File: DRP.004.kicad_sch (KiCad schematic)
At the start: 0 parts

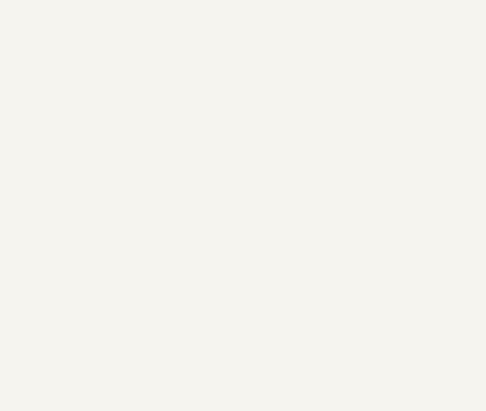
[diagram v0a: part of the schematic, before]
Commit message: Adjusted stencil for custom jig
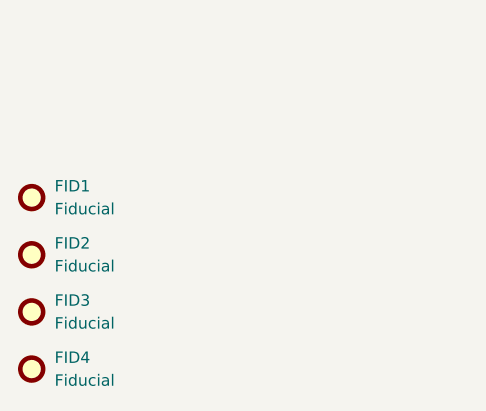
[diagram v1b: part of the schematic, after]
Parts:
- added FID1, FID2, FID3, FID4: Fiducial, Fiducial:Fiducial_0.5mm_Mask1.5mm, symbol Mechanical:Fiducial

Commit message: Finished v3
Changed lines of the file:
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@@
+		)
+	)
+	(symbol
+		(lib_id "Graphic:SYM_Flash_Large")
+		(at 254 156.21 0)
+		(unit 1)
+		(exclude_from_sim no)
+		(in_bom no)
+		(on_board yes)
+		(dnp no)
+		(property "Reference" "#SYM1"
+			(at 250.19 156.21 90)
+			(effects
+				(font
+					(size 1.27 1.27)
+				)
+				(hide yes)
+			)
+		)
+		(property "Value" "SYM_Flash_Large"
+			(at 257.302 156.21 90)
+			(effects
+				(font
+					(size 1.27 1.27)
+				)
+				(hide yes)
+			)
+		)
+		(property "Footprint" "Symbol:Symbol_HighVoltage_NoTriangle_2x5mm_Copper"
+			(at 253.238 163.576 0)
+			(effects
+				(font
+					(size 1.27 1.27)
+				)
+				(hide yes)
+			)
+		)
+		(property "Datasheet" "~"
+			(at 264.16 158.75 0)
+			(effects
+				(font
+					(size 1.27 1.27)
+				)
+				(hide yes)
+			)
+		)
+		(property "Description" "Flash symbol, large"
+			(at 254 156.21 0)
+			(effects
+				(font
+					(size 1.27 1.27)
+				)
+				(hide yes)
+			)
+		)
+		(property "Sim.Enable" "0"
+			(at 254 156.21 0)
+			(effects
+				(font
+					(size 1.27 1.27)
+				)
+				(hide yes)
+			)
+		)
+		(instances
+			(project ""
+				(path "/990f0ec4-1b5b-4db8-8f39-ecd88fffeea0"
+					(reference "#SYM1")
+					(unit 1)
+				)
+			)
 		)
 	)

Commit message: Expanded documentation
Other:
- note added: "${/990f0ec4-1b5b-4db8-8f39-ecd88fffeea0/6cce2e90-e51c-4942-a042-f4f9f078d271/66d2800e-8fce-4636-a04a-70d2094956bb:VALUE} Output: 3.0v - 4.4v Input USB: 5v Input BATT: 3.0v - 4.2v"
- note added: "${/990f0ec4-1b5b-4db8-8f39-ecd88fffeea0/9a8ba87a-c59f-4592-a0ef-e35d3bfde58d/a8d7b234-8ac0-468a-a976-6151f63ea50d:VALUE} FLASH: 32k RAM: 8k"
- note added: "1S Li-ion"
- note added: "BOOST ${/990f0ec4-1b5b-4db8-8f39-ecd88fffeea0/6cce2e90-e51c-4942-a042-f4f9f078d271/1bd17bee-2f02-427f-b24e-c0fc4b2c4825:VALUE} 5.5v"
- note added: "BUTTON"
- note added: "LDO ${/990f0ec4-1b5b-4db8-8f39-ecd88fffeea0/6cce2e90-e51c-4942-a042-f4f9f078d271/c47a5d3b-33a9-403c-a3ad-31fcb81bff44:VALUE} 1.8v 600mA"
- note added: "LEDs"
- note added: "SERVO"
- note added: "Slider switch + Power latch"
- note added: "USB"

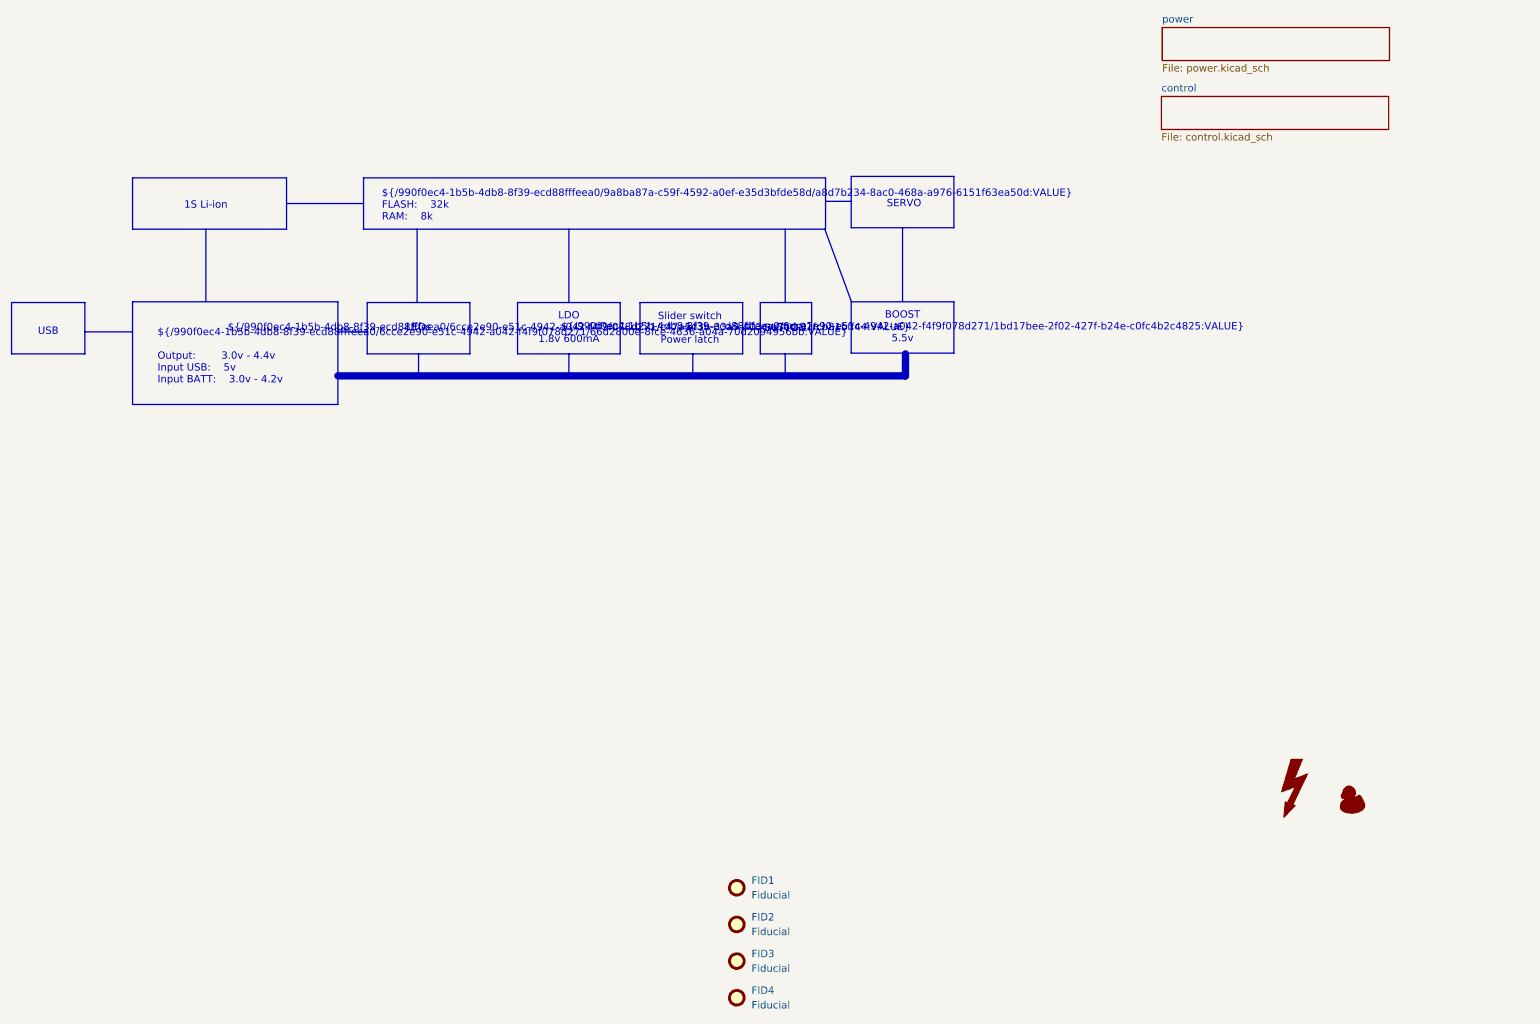
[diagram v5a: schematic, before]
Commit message: Updated schematics. Calculated inductor values
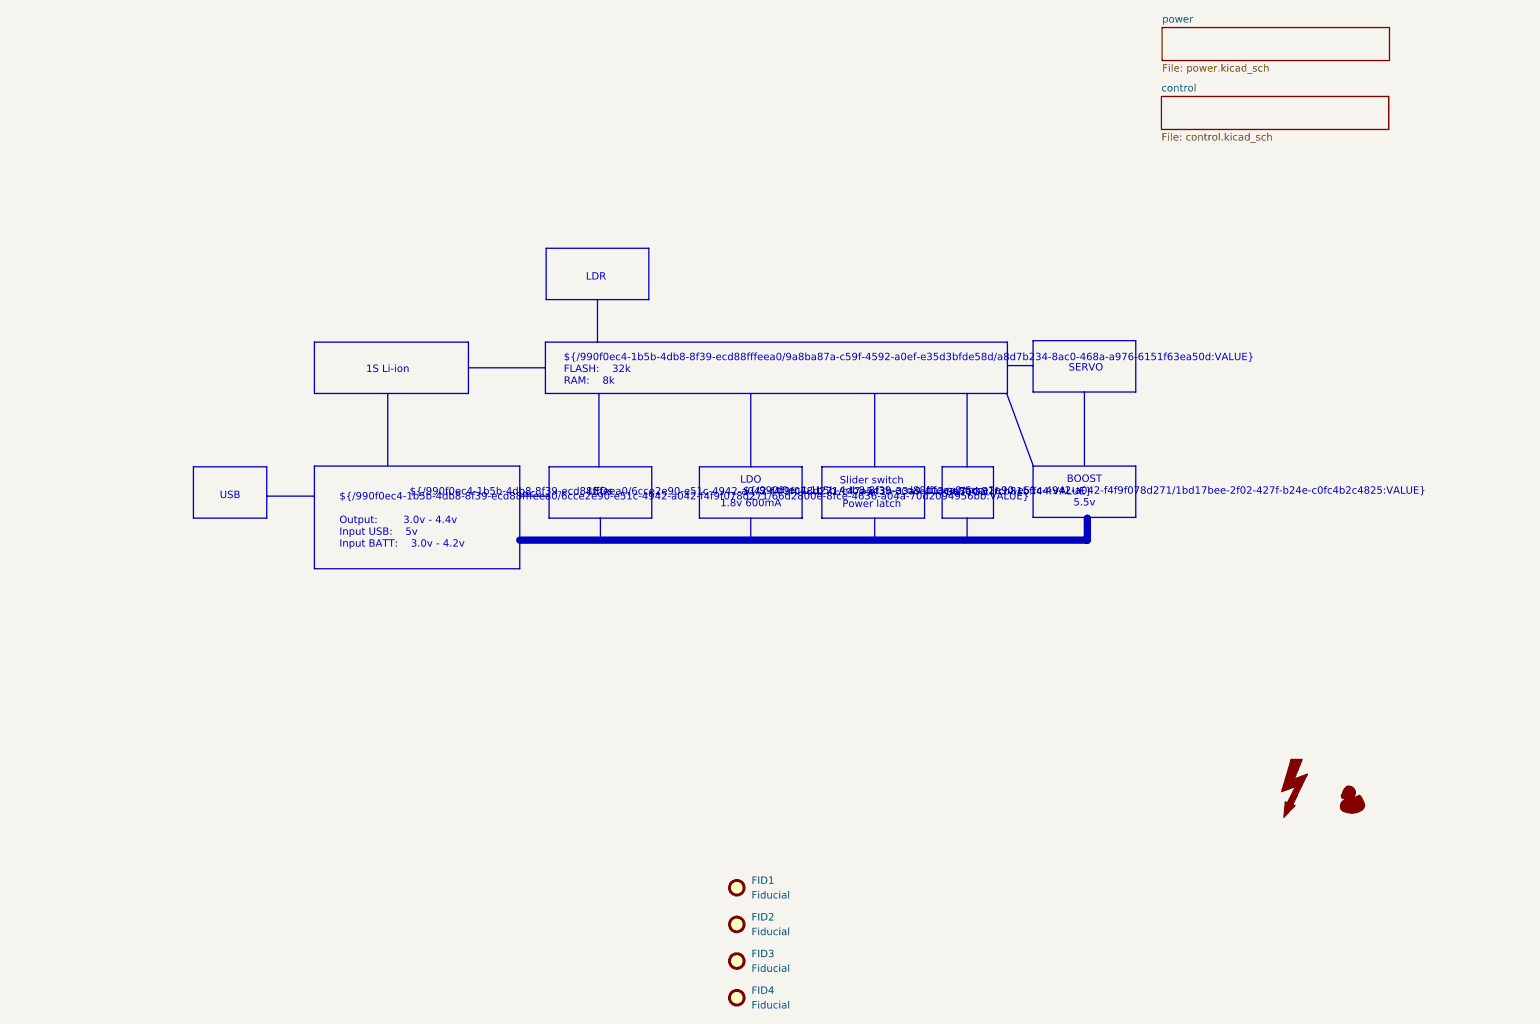
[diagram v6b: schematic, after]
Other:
- note added: "LDR"
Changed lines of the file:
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@@
 	)
 	(rectangle
-		(start 52.832 51.054)
-		(end 79.502 59.944)
+		(start 84.328 79.502)
+		(end 110.998 88.392)
 		(stroke
 			(width 0)
@@
 	)
 	(rectangle
-		(start 177.292 72.517)
-		(end 195.072 81.407)
+		(start 208.788 100.965)
+		(end 226.568 109.855)
 		(stroke
 			(width 0)
@@
 	)
 	(rectangle
-		(start 52.832 72.517)
-		(end 88.392 90.297)
+		(start 84.328 100.965)
+		(end 119.888 118.745)
 		(stroke
 			(width 0)
@@
 	)
 	(rectangle
-		(start 177.292 50.8)
-		(end 195.072 59.69)
+		(start 208.788 79.248)
+		(end 226.568 88.138)
 		(stroke
 			(width 0)
@@
 	)
 	(rectangle
-		(start 31.877 72.644)
-		(end 44.577 81.534)
+		(start 63.373 101.092)
+		(end 76.073 109.982)
 		(stroke
 			(width 0)
@@
 	)
 	(rectangle
-		(start 119.507 72.644)
-		(end 137.287 81.534)
+		(start 151.003 101.092)
+		(end 168.783 109.982)
 		(stroke
 			(width 0)
@@
 	)
 	(rectangle
-		(start 93.472 72.644)
-		(end 111.252 81.534)
+		(start 124.968 101.092)
+		(end 142.748 109.982)
 		(stroke
 			(width 0)
@@
 	)
 	(rectangle
-		(start 161.544 72.644)
-		(end 170.434 81.534)
+		(start 193.04 101.092)
+		(end 201.93 109.982)
 		(stroke
 			(width 0)
@@
 	)
 	(rectangle
-		(start 92.837 51.054)
-		(end 172.847 59.944)
+		(start 124.333 79.502)
+		(end 204.343 88.392)
 		(stroke
 			(width 0)
@@
 	)
 	(rectangle
-		(start 140.716 72.644)
-		(end 158.496 81.534)
+		(start 124.46 63.246)
+		(end 142.24 72.136)
+		(stroke
+			(width 0)
+			(type solid)
+			(color 0 194 194 1)
+		)
+		(fill
+			(type none)
+		)
+	)
+	(rectangle
+		(start 172.212 101.092)
+		(end 189.992 109.982)
 		(stroke
 			(width 0)
@@
 	(text "Slider switch\n+\nPower latch"
 		(exclude_from_sim no)
-		(at 149.352 77.216 0)
+		(at 180.848 105.664 0)
 		(effects
 			(font
@@
 	(text "LEDs\n"
 		(exclude_from_sim no)
-		(at 102.362 77.089 0)
+		(at 133.858 105.537 0)
 		(effects
 			(font
@@
 	(text "SERVO"
 		(exclude_from_sim no)
-		(at 186.436 55.626 0)
+		(at 217.932 84.074 0)
 		(effects
 			(font
@@
 	(text "BOOST\n${/990f0ec4-1b5b-4db8-8f39-ecd88fffeea0/6cce2e90-e51c-4942-a042-f4f9f078d271/1bd17bee-2f02-427f-b24e-c0fc4b2c4825:VALUE}\n5.5v\n"
 		(exclude_from_sim no)
-		(at 186.182 76.962 0)
+		(at 217.678 105.41 0)
 		(effects
 			(font
@@
 	(text "USB\n"
 		(exclude_from_sim no)
-		(at 38.227 77.724 0)
+		(at 69.723 106.172 0)
 		(effects
 			(font
@@
 	(text "${/990f0ec4-1b5b-4db8-8f39-ecd88fffeea0/9a8ba87a-c59f-4592-a0ef-e35d3bfde58d/a8d7b234-8ac0-468a-a976-6151f63ea50d:VALUE}\nFLASH:	32k\nRAM:	8k"
 		(exclude_from_sim no)
-		(at 96.012 55.88 0)
+		(at 127.508 84.328 0)
 		(effects
 			(font
@@
 	(text "LDO\n${/990f0ec4-1b5b-4db8-8f39-ecd88fffeea0/6cce2e90-e51c-4942-a042-f4f9f078d271/c47a5d3b-33a9-403c-a3ad-31fcb81bff44:VALUE}\n1.8v 600mA\n"
 		(exclude_from_sim no)
-		(at 128.397 77.089 0)
+		(at 159.893 105.537 0)
 		(effects
 			(font
@@
 		)
 	)
+	(text "LDR"
+		(exclude_from_sim no)
+		(at 133.096 68.326 0)
+		(effects
+			(font
+				(size 1.27 1.27)
+				(color 0 194 194 1)
+			)
+		)
+	)
 	(text "${/990f0ec4-1b5b-4db8-8f39-ecd88fffeea0/6cce2e90-e51c-4942-a042-f4f9f078d271/66d2800e-8fce-4636-a04a-70d2094956bb:VALUE}\n\nOutput:		3.0v - 4.4v\nInput USB:	5v\nInput BATT:	3.0v - 4.2v"
 		(exclude_from_sim no)
-		(at 57.15 82.042 0)
+		(at 88.646 110.49 0)
 		(effects
 			(font
@@
 	(text "1S Li-ion"
 		(exclude_from_sim no)
-		(at 65.532 55.88 0)
+		(at 97.028 84.328 0)
 		(effects
 			(font
@@
 	(text "BUTTON"
 		(exclude_from_sim no)
-		(at 165.862 77.216 0)
+		(at 197.358 105.664 0)
 		(effects
 			(font
@@
 	(polyline
 		(pts
-			(xy 88.392 85.344) (xy 186.69 85.344)
+			(xy 119.888 113.792) (xy 218.186 113.792)
 		)
 		(stroke
@@
 	(polyline
 		(pts
-			(xy 137.414 77.216) (xy 140.716 77.216)
+			(xy 168.91 105.664) (xy 172.212 105.664)
 		)
 		(stroke
@@
 	(polyline
 		(pts
-			(xy 149.86 85.09) (xy 149.606 85.09)
+			(xy 181.356 113.538) (xy 181.102 113.538)
 		)
 		(stroke
@@
 	(polyline
 		(pts
-			(xy 172.72 59.944) (xy 172.72 59.944)
+			(xy 204.216 88.392) (xy 204.216 88.392)
 		)
 		(stroke
@@
 	(polyline
 		(pts
-			(xy 88.392 77.724) (xy 93.472 77.724)
+			(xy 119.888 106.172) (xy 124.968 106.172)
 		)
 		(stroke
@@
 	(polyline
 		(pts
-			(xy 186.182 59.69) (xy 186.182 72.39)
+			(xy 217.678 88.138) (xy 217.678 100.838)
 		)
 		(stroke
@@
 	(polyline
 		(pts
-			(xy 102.108 59.944) (xy 102.108 72.644)
+			(xy 133.604 88.392) (xy 133.604 101.092)
 		)
 		(stroke
@@
 	(polyline
 		(pts
-			(xy 165.862 81.534) (xy 165.862 85.344)
+			(xy 181.356 88.392) (xy 181.356 101.092)
+		)
+		(stroke
+			(width 0)
+			(type solid)
+			(color 0 194 0 1)
+		)
+	)
+	(polyline
+		(pts
+			(xy 197.358 109.982) (xy 197.358 113.792)
 		)
 		(stroke
@@
 	(polyline
 		(pts
-			(xy 165.862 59.944) (xy 165.862 72.644)
+			(xy 197.358 88.392) (xy 197.358 101.092)
 		)
 		(stroke
@@
 	(polyline
 		(pts
-			(xy 149.86 81.534) (xy 149.86 85.09)
+			(xy 181.356 109.982) (xy 181.356 113.538)
 		)
 		(stroke
@@
 	(polyline
 		(pts
-			(xy 128.397 59.944) (xy 128.397 72.644)
+			(xy 159.893 88.392) (xy 159.893 101.092)
 		)
 		(stroke
@@
 	(polyline
 		(pts
-			(xy 172.974 55.118) (xy 177.292 55.118)
+			(xy 204.47 83.566) (xy 208.788 83.566)
 		)
 		(stroke
@@
 	(polyline
 		(pts
-			(xy 177.292 72.39) (xy 172.72 59.944)
+			(xy 208.788 100.838) (xy 204.216 88.392)
 		)
 		(stroke
@@
 	(polyline
 		(pts
-			(xy 158.496 77.216) (xy 161.544 77.216)
+			(xy 189.992 105.664) (xy 193.04 105.664)
 		)
 		(stroke
@@
 	(polyline
 		(pts
-			(xy 137.16 59.69) (xy 137.16 59.69)
+			(xy 168.656 88.138) (xy 168.656 88.138)
 		)
 		(stroke
@@
 	(polyline
 		(pts
-			(xy 65.532 59.944) (xy 65.532 72.39)
+			(xy 97.028 88.392) (xy 97.028 100.838)
 		)
 		(stroke
@@
 	(polyline
 		(pts
-			(xy 44.577 77.724) (xy 52.832 77.724)
+			(xy 76.073 106.172) (xy 84.328 106.172)
 		)
 		(stroke
@@
 	(polyline
 		(pts
-			(xy 186.69 81.534) (xy 186.69 85.344)
+			(xy 218.186 109.982) (xy 218.186 113.792)
 		)
 		(stroke
@@
 	(polyline
 		(pts
-			(xy 102.362 81.534) (xy 102.362 85.344)
+			(xy 133.35 72.136) (xy 133.35 79.502)
+		)
+		(stroke
+			(width 0)
+			(type solid)
+			(color 0 194 194 1)
+		)
+	)
+	(polyline
+		(pts
+			(xy 133.858 109.982) (xy 133.858 113.792)
 		)
 		(stroke
@@
 	(polyline
 		(pts
-			(xy 128.397 81.534) (xy 128.397 85.344)
+			(xy 159.893 109.982) (xy 159.893 113.792)
 		)
 		(stroke
@@
 	(polyline
 		(pts
-			(xy 79.502 55.499) (xy 92.837 55.499)
+			(xy 110.998 83.947) (xy 124.333 83.947)
 		)
 		(stroke
@@
 	)
 	(image
-		(at 57.15 154.305)
-		(scale 0.365906)
+		(at 277.114 174.117)
+		(scale 0.0894668)
 		(data "iVBORw0KGgoAAAANSUhEUgAAAgAAAAIACAYAAAD0eNT6AAAACXBIWXMAAAsTAAALEwEAmpwYAAAA"
 			"AXNSR0IArs4c6QAAAARnQU1BAACxjwv8YQUAApSRSURBVHgB7P150GTXdR8Innvfy/yWWlFVKKCw"
@@
 			)
 		)
+		(property "Tolerance " ""
+			(at 157.48 180.34 0)
+			(effects
+				(font
+					(size 1.27 1.27)
+				)
+				(hide yes)
+			)
+		)
 		(instances
 			(project "DRP.004"
@@
 			)
 		)
+		(property "Tolerance " ""
+			(at 157.48 186.69 0)
+			(effects
+				(font
+					(size 1.27 1.27)
+				)
+				(hide yes)
+			)
+		)
 		(instances
 			(project "DRP.004"
@@
 			)
 		)
+		(property "Tolerance " ""
+			(at 157.48 173.99 0)
+			(effects
+				(font
+					(size 1.27 1.27)
+				)
+				(hide yes)
+			)
+		)
 		(instances
 			(project ""
@@
 			)
 		)
+		(property "Tolerance " ""
+			(at 157.48 193.04 0)
+			(effects
+				(font
+					(size 1.27 1.27)
+				)
+				(hide yes)
+			)
+		)
 		(instances
 			(project "DRP.004"
@@
 			(at 254 156.21 0)
 			(effects
-				(font
-					(size 1.27 1.27)
-				)
-				(hide yes)
-			)
-		)
-		(property "Sim.Enable" "0"
-			(at 254 156.21 0)
-			(effects
